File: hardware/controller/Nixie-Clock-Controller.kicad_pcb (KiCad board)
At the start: 2 copper layers, 63 parts, among them IC1 ESP32-DEVKITC-V4, IC2 74141, J1 9/12-35V DC in, J2 Nixies-Connector, J3 Buttons, J4 Buzzer, Q1 MPSA42, Q10 MPSA42, Q11 MPSA42, Q12 MPSA42, Q13 MPSA42, Q14 MPSA42, Q2 MPSA92, Q3 MPSA92, Q4 MPSA92, Q5 MPSA92, Q6 MPSA92, Q7 MPSA92, Q8 MPSA92, Q9 MPSA42, SW1 on/off, SW2 in voltage select, U1 L7805, U2 L7809, U3 NCH6300HV

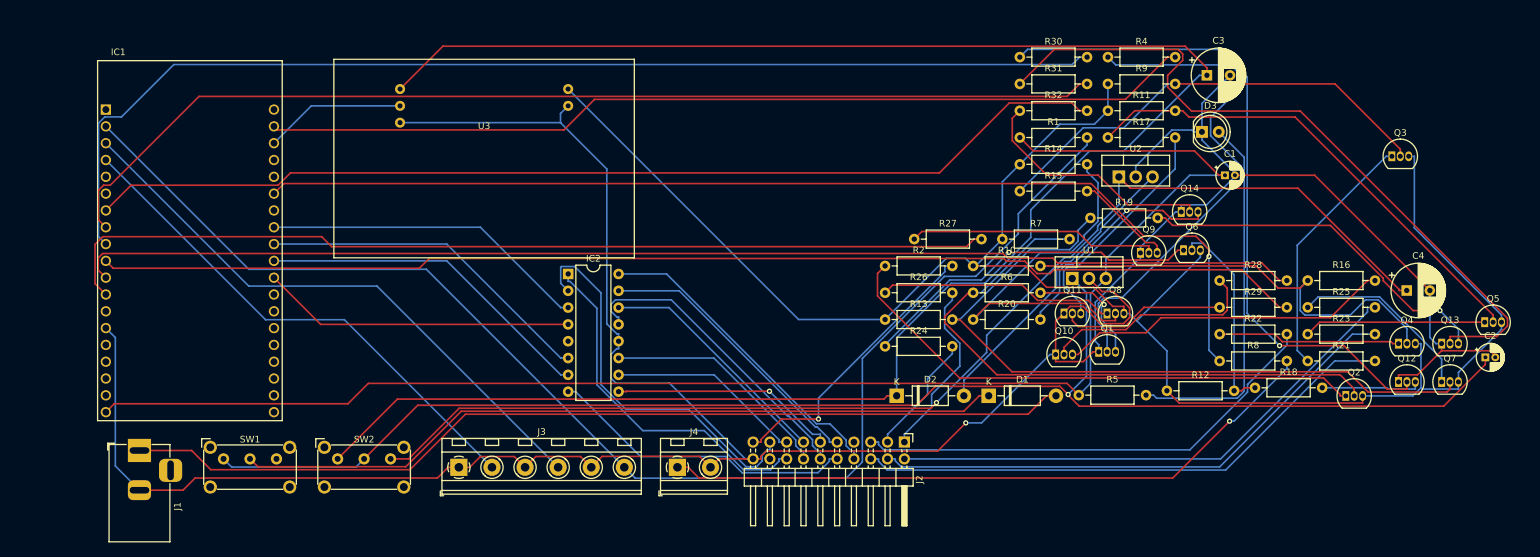
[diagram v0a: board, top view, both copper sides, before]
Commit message: Add screw terminals for I/O, Improve PCB layout
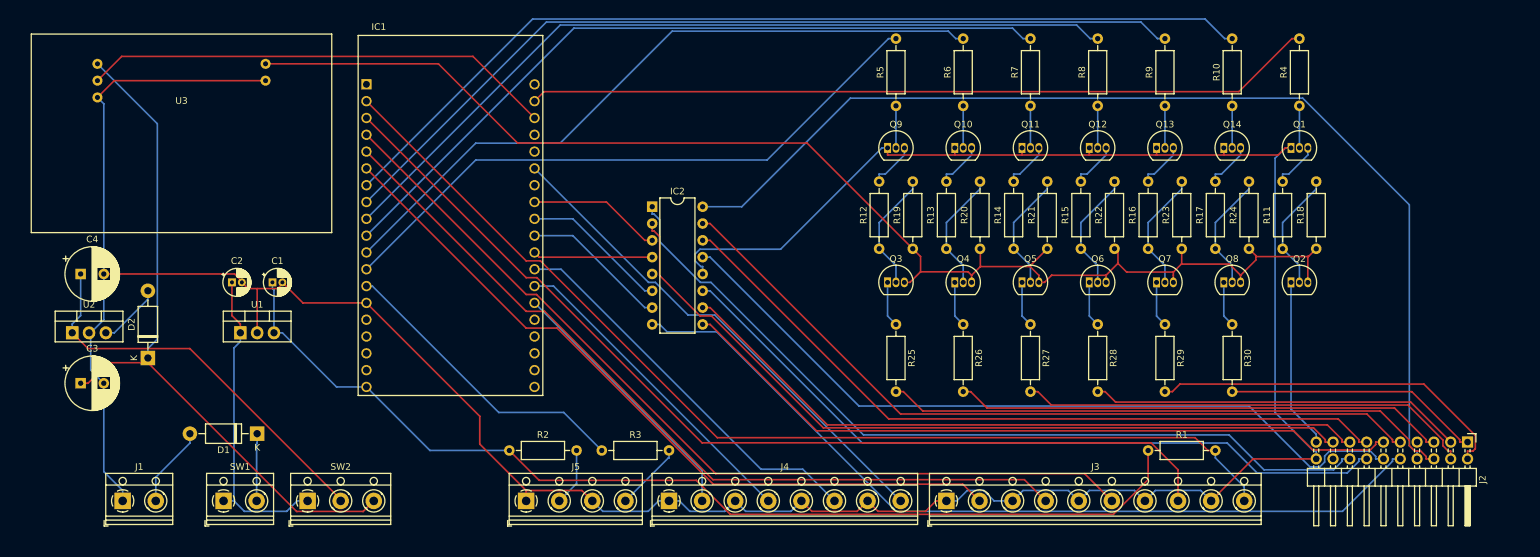
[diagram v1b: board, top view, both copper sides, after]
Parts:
- removed D3: power-LED, LED_THT:LED_D5.0mm
- removed R31, R32: 33k, Resistor_THT:R_Axial_DIN0207_L6.3mm_D2.5mm_P10.16mm_Horizontal
- added J5: LEDs, TerminalBlock_RND:TerminalBlock_RND_205-00014_1x04_P5.00mm_Horizontal, F.Cu at (91.4, 87.6)
- added R3: 220R, Resistor_THT:R_Axial_DIN0207_L6.3mm_D2.5mm_P10.16mm_Horizontal, F.Cu at (102.9, 80.0)
- J1: footprint Connector_BarrelJack:BarrelJack_Horizontal -> TerminalBlock_RND:TerminalBlock_RND_205-00012_1x02_P5.00mm_Horizontal
- J3: value Buttons -> Input; footprint TerminalBlock_MetzConnect:TerminalBlock_MetzConnect_Type094_RT03506HBLU_1x06_P5.00mm_Horizontal -> TerminalBlock_RND:TerminalBlock_RND_205-00020_1x10_P5.00mm_Horizontal
- J4: value Buzzer -> Output; footprint TerminalBlock_MetzConnect:TerminalBlock_MetzConnect_Type094_RT03502HBLU_1x02_P5.00mm_Horizontal -> TerminalBlock_RND:TerminalBlock_RND_205-00018_1x08_P5.00mm_Horizontal
- R10, R7, R9: value 100k -> 33k
- R11, R12, R13, R14: value 100k -> 470k
- R18, R19, R20: value 470k -> 100k
- R2: value 15k -> 220R
- R21, R22, R23, R24: value 15k -> 100k
- R25, R26: value 15k -> 10k
- R27, R28, R29, R30: value 33k -> 10k
- R5: value 220R -> 33k
- R6: value 470k -> 33k
- R8: value 100R -> 33k
- SW1: footprint Button_Switch_THT:SW_E-Switch_EG1224_SPDT_Angled -> TerminalBlock_RND:TerminalBlock_RND_205-00012_1x02_P5.00mm_Horizontal
- SW2: footprint Button_Switch_THT:SW_E-Switch_EG1224_SPDT_Angled -> TerminalBlock_RND:TerminalBlock_RND_205-00013_1x03_P5.00mm_Horizontal
- moved C4 200.4 mm to (24.1, 53.3)
- moved C2 189.7 mm to (47.0, 54.6)
- moved C3 176.4 mm to (24.1, 69.8)
- moved U2 159.9 mm to (22.9, 62.2)
- moved C1 144.8 mm to (53.1, 54.6)
- moved U1 126.0 mm to (48.3, 62.2)
- moved D2 113.3 mm to (34.3, 66.0), turned to 90 degrees
- moved D1 110.7 mm to (50.8, 77.5), turned to 180 degrees
- moved J2 85.1 mm to (233.7, 78.7)
- moved Q3 78.5 mm to (146.1, 54.6)
- moved J3 73.8 mm to (154.9, 87.6)
- moved Q5 70.2 mm to (166.4, 54.6)
- moved Q4 67.7 mm to (156.2, 54.6)
- moved R2 63.3 mm to (88.9, 80.0)
- moved R25 62.3 mm to (147.3, 61.0), turned to 270 degrees
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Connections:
- IC1 pad 1: Net-(IC1-Pad1) -> (no net)
- IC1 pad 15: Net-(IC1-Pad15) -> (no net)
- IC1 pad 16: Net-(IC1-Pad16) -> (no net)
- IC1 pad 17: Net-(IC1-Pad17) -> (no net)
- IC1 pad 18: Net-(IC1-Pad18) -> (no net)
- IC1 pad 20: Net-(IC1-Pad20) -> (no net)
- IC1 pad 23: Net-(IC1-Pad23) -> (no net)
- IC1 pad 24: Net-(IC1-Pad24) -> (no net)
- IC1 pad 25: Net-(IC1-Pad25) -> /out_1
- IC1 pad 26: Net-(IC1-Pad26) -> (no net)
- IC1 pad 3: /b_hour -> /in_1
- IC1 pad 31: Net-(IC1-Pad31) -> /out_2
- IC1 pad 32: Net-(IC1-Pad32) -> /out_3
- IC1 pad 33: Net-(IC1-Pad33) -> /out_4
- IC1 pad 34: Net-(IC1-Pad34) -> (no net)
- IC1 pad 35: Net-(IC1-Pad35) -> (no net)
- IC1 pad 36: Net-(IC1-Pad36) -> (no net)
- IC1 pad 37: Net-(IC1-Pad37) -> (no net)
- IC1 pad 38: Net-(IC1-Pad38) -> (no net)
- IC1 pad 4: /b_min -> /in_2
- IC1 pad 5: Net-(IC1-Pad5) -> /in_3
- IC1 pad 6: Net-(IC1-Pad6) -> /in_4
- IC2 pad 5: +5V -> (no net)
- J1 pad 1: Net-(D1-Pad2) -> GND
- J1 pad 2: GND -> Net-(D1-Pad2)
- J2 pad 18: Net-(J2-Pad18) -> (no net)
- J2 pad 7: Net-(J2-Pad7) -> (no net)
- J3 pad 2: /b_min -> /in_4
- J3 pad 4: /b_hour -> /in_3
- J3 pad 6: /b_reset -> /in_2
- J4 pad 1: Net-(J4-Pad1) -> GND
- J4 pad 2: GND -> /out_4
- Q2 pad 1: Net-(Q2-Pad1) -> /da
- R10 pad 1: Net-(Q2-Pad3) -> Net-(Q14-Pad2)
- R10 pad 2: Net-(Q4-Pad2) -> Net-(IC1-Pad7)
- R11 pad 1: Net-(Q2-Pad3) -> Net-(Q2-Pad2)
- R11 pad 2: Net-(Q5-Pad2) -> Net-(Q1-Pad3)
- R12 pad 1: Net-(Q2-Pad3) -> Net-(Q3-Pad2)
- R12 pad 2: Net-(Q6-Pad2) -> Net-(Q9-Pad3)
- R13 pad 1: Net-(Q2-Pad3) -> Net-(Q4-Pad2)
- R13 pad 2: Net-(Q7-Pad2) -> Net-(Q10-Pad3)
- R14 pad 1: Net-(Q2-Pad3) -> Net-(Q5-Pad2)
- R14 pad 2: Net-(Q8-Pad2) -> Net-(Q11-Pad3)
- R15 pad 1: Net-(Q3-Pad2) -> Net-(Q6-Pad2)
- R15 pad 2: Net-(Q9-Pad3) -> Net-(Q12-Pad3)
- R16 pad 1: Net-(Q4-Pad2) -> Net-(Q7-Pad2)
- R16 pad 2: Net-(Q10-Pad3) -> Net-(Q13-Pad3)
- R17 pad 1: Net-(Q5-Pad2) -> Net-(Q8-Pad2)
- R17 pad 2: Net-(Q11-Pad3) -> Net-(Q14-Pad3)
- R18 pad 1: Net-(Q6-Pad2) -> Net-(Q2-Pad3)
- R18 pad 2: Net-(Q12-Pad3) -> Net-(Q2-Pad2)
- R19 pad 1: Net-(Q7-Pad2) -> Net-(Q2-Pad3)
- R19 pad 2: Net-(Q13-Pad3) -> Net-(Q3-Pad2)
- R2 pad 1: Net-(Q2-Pad1) -> Net-(C1-Pad1)
- R2 pad 2: /da -> Net-(J5-Pad2)
- R20 pad 1: Net-(Q8-Pad2) -> Net-(Q2-Pad3)
- R20 pad 2: Net-(Q14-Pad3) -> Net-(Q4-Pad2)
- R21 pad 1: Net-(Q3-Pad1) -> Net-(Q2-Pad3)
- R21 pad 2: /a6 -> Net-(Q5-Pad2)
- R22 pad 1: Net-(Q4-Pad1) -> Net-(Q2-Pad3)
- R22 pad 2: /a5 -> Net-(Q6-Pad2)
- R23 pad 1: Net-(Q5-Pad1) -> Net-(Q2-Pad3)
- R23 pad 2: /a4 -> Net-(Q7-Pad2)
- R24 pad 1: Net-(Q6-Pad1) -> Net-(Q2-Pad3)
- R24 pad 2: /a3 -> Net-(Q8-Pad2)
- R25 pad 1: Net-(Q7-Pad1) -> Net-(Q3-Pad1)
- R25 pad 2: /a2 -> /a6
- R26 pad 1: Net-(Q8-Pad1) -> Net-(Q4-Pad1)
- R26 pad 2: /a1 -> /a5
- R27 pad 1: Net-(Q9-Pad2) -> Net-(Q5-Pad1)
- R27 pad 2: Net-(IC1-Pad12) -> /a4
- R28 pad 1: Net-(Q10-Pad2) -> Net-(Q6-Pad1)
- R28 pad 2: Net-(IC1-Pad11) -> /a3
- R29 pad 1: Net-(Q11-Pad2) -> Net-(Q7-Pad1)
- R29 pad 2: Net-(IC1-Pad10) -> /a2
- R30 pad 1: Net-(Q12-Pad2) -> Net-(Q8-Pad1)
- R30 pad 2: Net-(IC1-Pad9) -> /a1
- R5 pad 1: Net-(C1-Pad1) -> Net-(Q9-Pad2)
- R5 pad 2: Net-(D3-Pad2) -> Net-(IC1-Pad12)
- R6 pad 1: Net-(Q2-Pad2) -> Net-(Q10-Pad2)
- R6 pad 2: Net-(Q1-Pad3) -> Net-(IC1-Pad11)
- R7 pad 1: Net-(Q2-Pad3) -> Net-(Q11-Pad2)
- R7 pad 2: Net-(Q2-Pad2) -> Net-(IC1-Pad10)
- R8 pad 1: Net-(IC1-Pad25) -> Net-(Q12-Pad2)
- R8 pad 2: Net-(J4-Pad1) -> Net-(IC1-Pad9)
- R9 pad 1: Net-(Q2-Pad3) -> Net-(Q13-Pad2)
- R9 pad 2: Net-(Q3-Pad2) -> Net-(IC1-Pad8)
- SW2 pad 1: Net-(C3-Pad1) -> Net-(C2-Pad1)
- SW2 pad 2: Net-(C2-Pad1) -> Net-(C4-Pad1)
- SW2 pad 3: Net-(C4-Pad1) -> Net-(C3-Pad1)
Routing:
- net Net-(C3-Pad1): track 290.0 -> 105.0 mm
- net Net-(C2-Pad1): track 220.8 -> 48.0 mm, vias 1 -> 0
- net Net-(IC1-Pad25): track 163.5 -> 0.00 mm, vias 1 -> 0
- net /in_1: track 0.00 -> 149.4 mm
- net /in_2: track 0.00 -> 135.5 mm
- net Net-(D1-Pad2): track 144.3 -> 12.3 mm
- net /in_3: track 0.00 -> 124.5 mm
- net Net-(C4-Pad1): track 182.7 -> 60.6 mm, vias 1 -> 0
- net /in_4: track 0.00 -> 113.4 mm
- net /c0: track 48.3 -> 159.3 mm
- net Net-(D1-Pad1): track 116.5 -> 10.2 mm
- net Net-(Q13-Pad2): track 110.4 -> 6.35 mm
- net Net-(J4-Pad1): track 100.7 -> 0.00 mm, vias 1 -> 0
- net Net-(Q12-Pad2): track 102.2 -> 6.35 mm, vias 1 -> 0
- net Net-(Q7-Pad2): track 109.2 -> 18.4 mm
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
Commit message: Add Mounting Holes to PCB, Improve Routing, Add power pin header, Use correct connector footprint
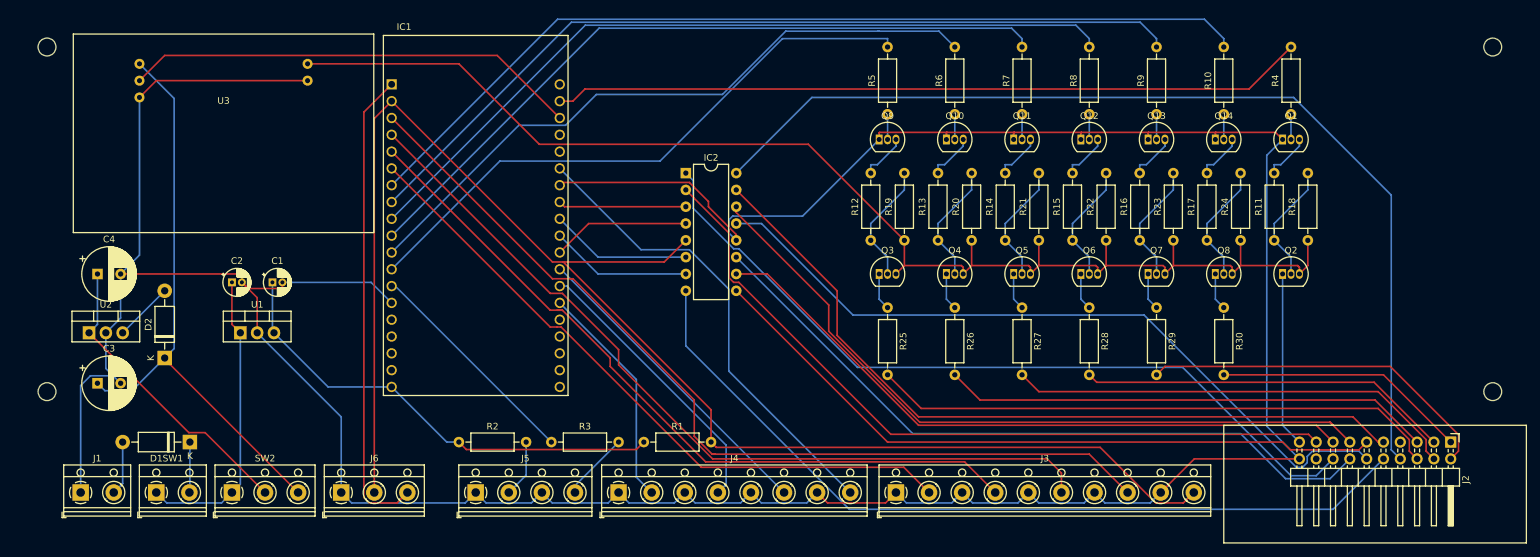
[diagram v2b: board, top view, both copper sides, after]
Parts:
- added H1: MountingHole, MountingHole:MountingHole_2.7mm_M2.5, F.Cu at (19.1, 19.1)
- added H2: MountingHole, MountingHole:MountingHole_2.7mm_M2.5, F.Cu at (237.5, 19.1)
- added H3: MountingHole, MountingHole:MountingHole_2.7mm_M2.5, F.Cu at (19.1, 71.1)
- added H4: MountingHole, MountingHole:MountingHole_2.7mm_M2.5, F.Cu at (237.5, 71.1)
- added J6: power_out, TerminalBlock_RND:TerminalBlock_RND_205-00013_1x03_P5.00mm_Horizontal, F.Cu at (63.5, 86.4)
- J2: footprint Connector_PinHeader_2.54mm:PinHeader_2x10_P2.54mm_Horizontal -> nixie-clock:PinHeader_2x10_P2.54mm_Horizontal_with_Interlock
- moved R1 76.2 mm to (109.2, 78.7)
- moved SW2 11.5 mm to (47.0, 86.4)
- moved D1 10.2 mm to (40.6, 78.7)
- moved SW1 10.2 mm to (35.6, 86.4)
- moved R2 7.73 mm to (81.3, 78.7)
- moved R3 7.73 mm to (95.2, 78.7)
- moved J3 7.73 mm to (147.3, 86.4)
- moved J4 7.73 mm to (105.4, 86.4)
- moved J5 7.73 mm to (83.8, 86.4)
- moved IC2 7.18 mm to (115.6, 38.1)
- moved J1 6.48 mm to (24.1, 86.4)
- moved U3 6.35 mm to (38.1, 26.7)
- moved IC1 3.81 mm to (83.8, 44.5)
- moved R28 2.84 mm to (176.5, 58.4)
- moved R29 2.84 mm to (186.7, 58.4)
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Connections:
- IC1 pad 1: (no net) -> Net-(IC1-Pad1)
- IC1 pad 2: /b_reset -> VCC
- IC1 pad 26: (no net) -> GND
- IC2 pad 5: (no net) -> VCC
- J3 pad 10: /b_reset -> VCC
- R1 pad 2: /b_reset -> VCC
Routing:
- net VCC: track 0.00 -> 229.9 mm
- net /b_reset: track 159.6 -> 0.00 mm
- net Net-(C1-Pad1): track 157.7 -> 71.4 mm
- net Net-(IC1-Pad1): track 0.00 -> 71.7 mm
- net GND: track 472.9 -> 520.1 mm
- net Net-(C3-Pad1): track 105.0 -> 88.5 mm
- net Net-(C4-Pad1): track 60.6 -> 46.0 mm
- net Net-(IC1-Pad13): track 45.8 -> 33.9 mm
- net /in_4: track 113.4 -> 101.5 mm
- net /out_2: track 59.8 -> 47.9 mm
- net /in_1: track 149.4 -> 138.2 mm
- net /in_3: track 124.5 -> 114.1 mm
- net /c0: track 159.3 -> 150.2 mm
- net /in_2: track 135.5 -> 126.7 mm
- net /out_4: track 40.4 -> 34.4 mm
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
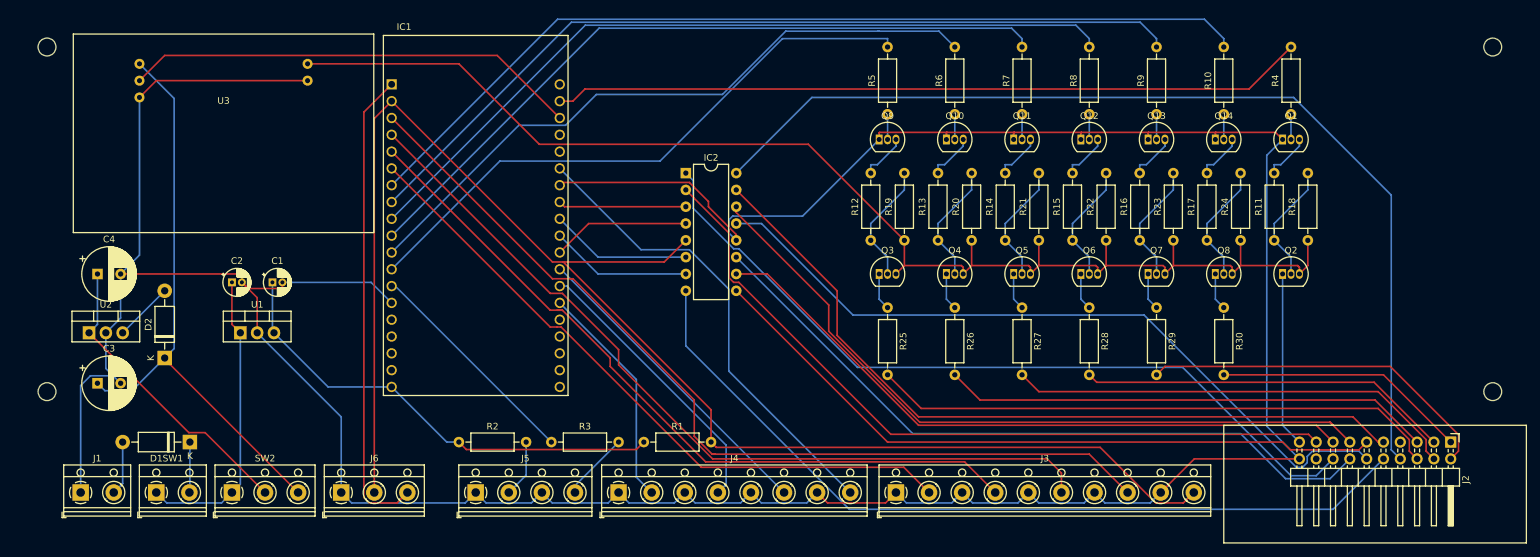
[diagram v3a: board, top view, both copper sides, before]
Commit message: Shrink pcbs
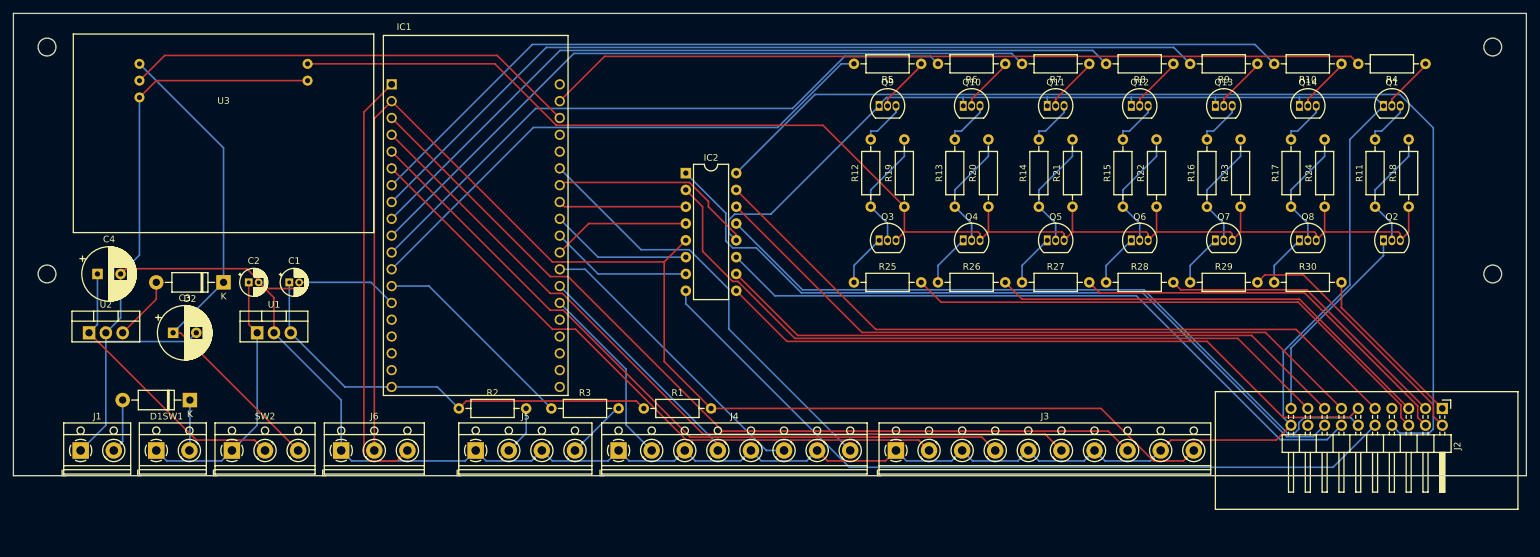
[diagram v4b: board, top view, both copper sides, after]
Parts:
- moved R4 21.7 mm to (227.3, 21.6), turned to 180 degrees
- moved R10 19.3 mm to (214.6, 21.6), turned to 180 degrees
- moved H3 17.8 mm to (19.1, 53.3)
- moved H4 17.8 mm to (237.5, 53.3)
- moved R9 17.0 mm to (201.9, 21.6), turned to 180 degrees
- moved R11 16.1 mm to (219.7, 43.2)
- moved Q2 16.1 mm to (221.0, 48.3)
- moved Q1 16.1 mm to (221.0, 27.9)
- moved R18 16.1 mm to (224.8, 43.2)
- moved R8 14.8 mm to (189.2, 21.6), turned to 180 degrees
- moved D2 14.5 mm to (45.7, 54.6), turned to 180 degrees
- moved C3 13.7 mm to (38.1, 62.2)
- moved R24 13.7 mm to (212.1, 43.2)
- moved Q14 13.7 mm to (208.3, 27.9)
- moved Q8 13.7 mm to (208.3, 48.3)
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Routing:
- net VCC: track 229.9 -> 212.5 mm
- net GND: track 520.1 -> 536.1 mm
- net /a2: track 54.6 -> 38.8 mm
- net /c0: track 150.2 -> 164.8 mm
- net Net-(C3-Pad1): track 88.5 -> 75.3 mm
- net Net-(Q2-Pad3): track 200.5 -> 213.6 mm
- net /a1: track 38.5 -> 25.4 mm
- net /a3: track 56.3 -> 46.0 mm
- net Net-(IC1-Pad21): track 113.9 -> 123.9 mm
- net /c2: track 127.1 -> 119.0 mm
- net /out_3: track 42.8 -> 34.7 mm
- net Net-(IC1-Pad12): track 90.6 -> 82.7 mm
- net /a4: track 68.5 -> 60.8 mm
- net /c1: track 117.5 -> 110.2 mm
- net /c5: track 110.9 -> 104.1 mm
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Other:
- board outline added: 228.6 x 69.8 mm
